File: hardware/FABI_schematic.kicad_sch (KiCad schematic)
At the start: 63 parts, among them J1 Conn_01x02_Pin, J11_GND1 Conn_01x01_Male, J11_VDD1 Conn_01x01_Male, J11_data1 Conn_01x01_Male, J12 Conn_01x04_Socket, J2 display_connector_91601-304LF, J3 54601-906WPLF, J4 54-00174 / FC68125, J5 54-00174 / FC68125, J6 009159005551906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

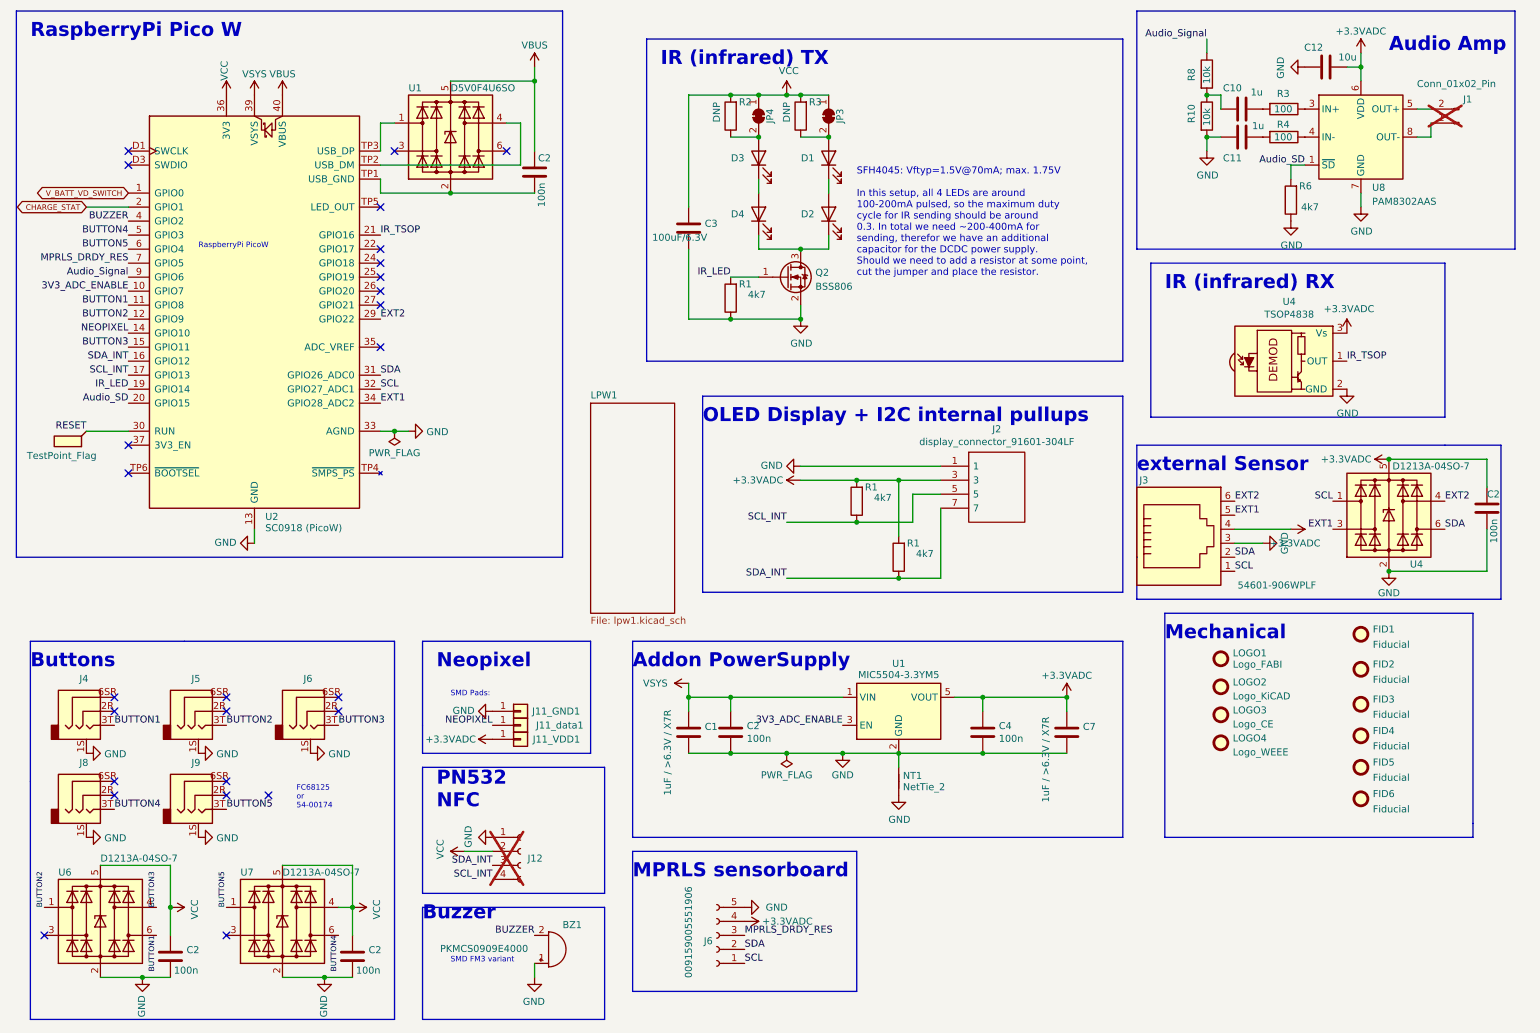
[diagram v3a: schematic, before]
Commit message: Changed pins for J3 connector as it's sufficient to have I2C1 (GP18, GP19) for SDA/SCL, does not need ADC; V_BATT_MEASURE now uses GP28 with the built-in ADC; Connector J12 now uses 3.3V as well (from VCC); Improved layout;
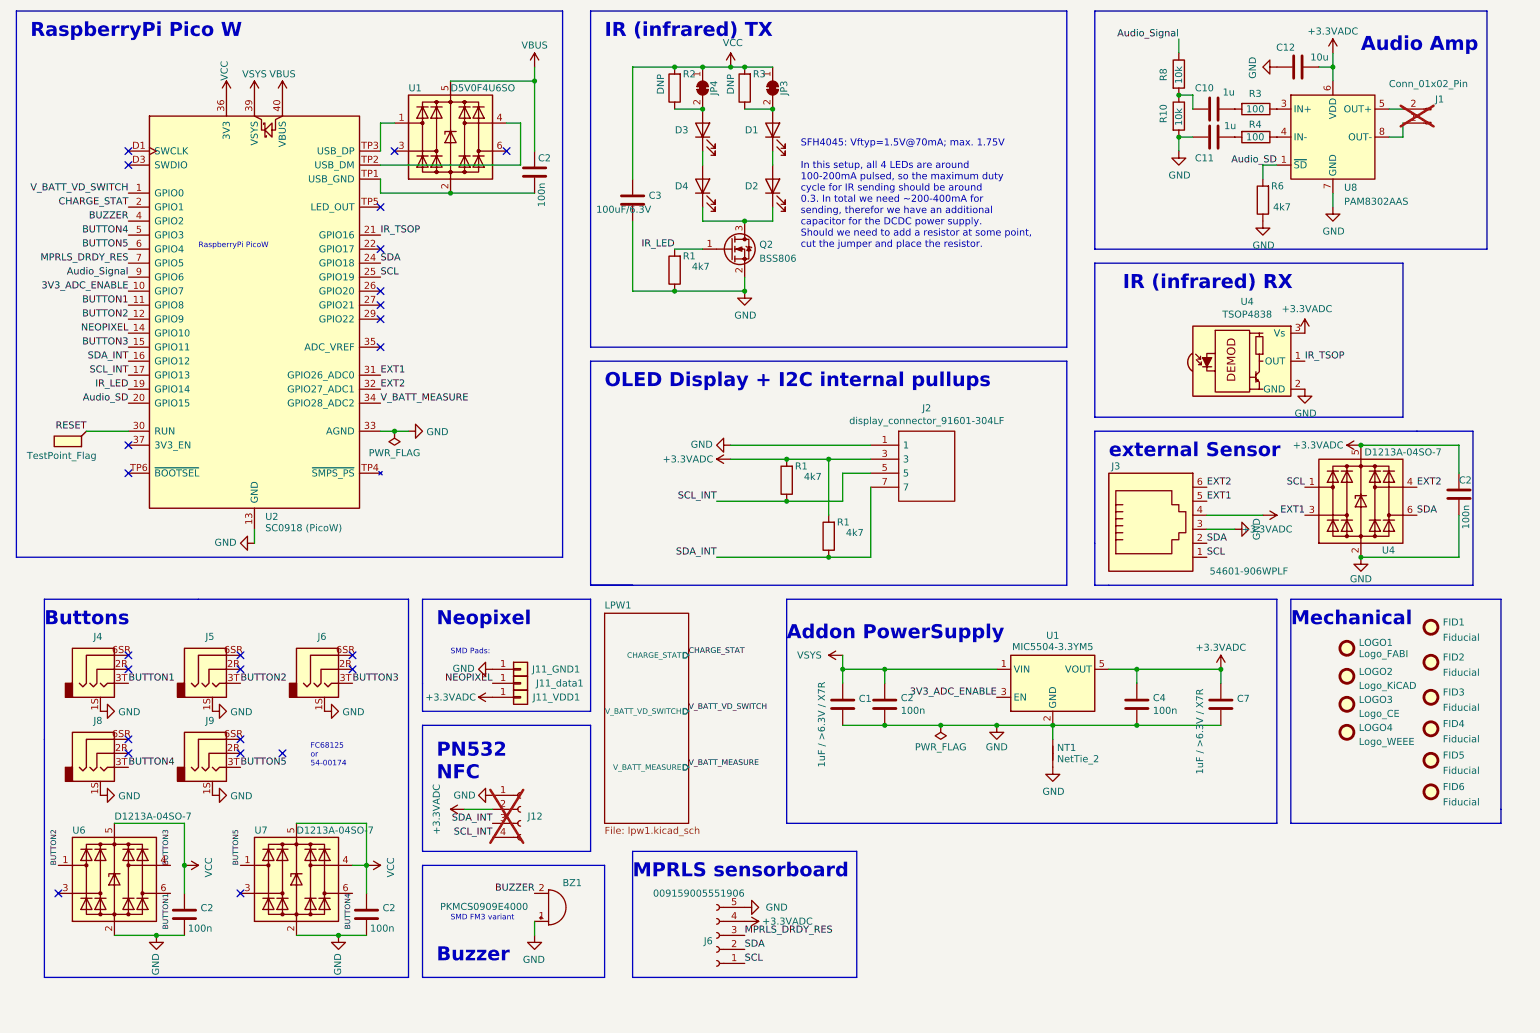
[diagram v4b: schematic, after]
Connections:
- net +3.3VADC: now also J12.2 (Pin_2)
- net EXT1: now also U2.31 (GPIO26_ADC0); no longer U2.34 (GPIO28_ADC2)
- net EXT2: now also U2.32 (GPIO27_ADC1); no longer U2.29 (GPIO22)
- net SCL: now also U2.25 (GPIO19); no longer U2.32 (GPIO27_ADC1)
- net SDA: now also U2.24 (GPIO18); no longer U2.31 (GPIO26_ADC0)
- net VCC: no longer J12.2 (Pin_2)
- new net V_BATT_MEASURE: U2.34 (GPIO28_ADC2)
- no-connect marks 26 -> 25
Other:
- sheet LPW1 ports: added CHARGE_STAT, V_BATT_MEASURE, V_BATT_VD_SWITCH; removed none
- moved on the sheet: BZ1, C1, C10, C11, C12, C2, C3, C4, C7, D1, D2, D3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

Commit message: Removed PWR_FLAGS except for VSYS; Removed NT2 (obsolete); Updated Schematics PDF; Reduced V_PWR_SWITCH routes to 1 from 2 to make space for VCC due to it being routed around the mounting holes of connectors J8/9; Improved silkscreen; TVS Diodes routes size increased; Updated BOM;
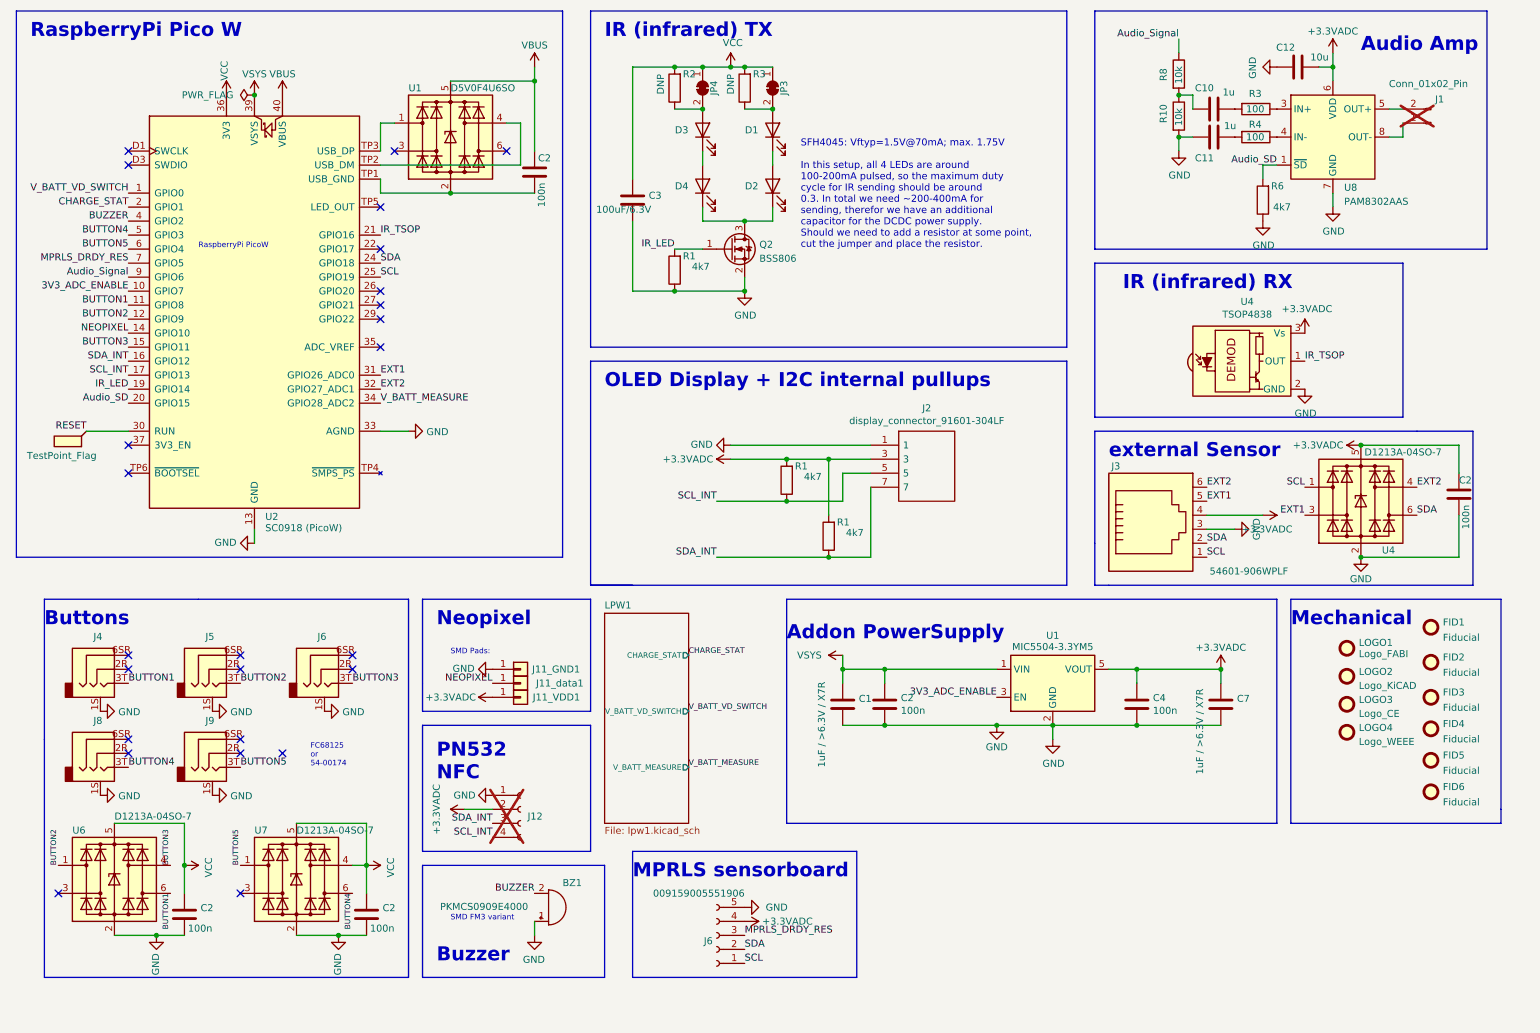
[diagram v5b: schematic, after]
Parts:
- removed NT1: NetTie_2, NetTie:NetTie-2_SMD_Pad0.5mm, symbol Device:NetTie_2
- J2: Mouser (none) -> 649-91601-304LF
- R10, R8: Mouser Part Number (none) -> 71-RCA060310K0FKEA
- R3, R4: Mouser (none) -> 667-ERJ-3EKF1000V
- U1: Mouser Part Number (none) -> 621-D5V0F4U6SO-7
- U4: Mouser Part Number (none) -> 782-TSOP4838
- U8: Mouser Part Number (none) -> 621-PAM8302AASCR
